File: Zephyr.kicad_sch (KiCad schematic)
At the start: 24 parts, among them J1 Conn_02x03_Counter_Clockwise, J11 Conn_01x03, SW4 SW_Push, U1 STM32F405RGT6, Y1 32.768KHz 12.5pF, Y2 8MHz 12pF

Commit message: Start ADC work
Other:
- added sheet ADC (adc_power.kicad_sch)
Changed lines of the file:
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@@
+	)
+	(sheet
+		(at 124.46 143.51)
+		(size 34.29 17.78)
+		(exclude_from_sim no)
+		(in_bom yes)
+		(on_board yes)
+		(dnp no)
+		(fields_autoplaced yes)
+		(stroke
+			(width 0.1524)
+			(type solid)
+		)
+		(fill
+			(color 0 0 0 0.0000)
+		)
+		(property "Sheetname" "ADC"
+			(at 124.46 142.7984 0)
+			(effects
+				(font
+					(size 1.27 1.27)
+				)
+				(justify left bottom)
+			)
+		)
+		(property "Sheetfile" "adc_power.kicad_sch"
+			(at 124.46 161.8746 0)
+			(effects
+				(font
+					(size 1.27 1.27)
+				)
+				(justify left top)
+			)
+		)
+		(instances
+			(project "Zephyr"
+				(path "/e99ca14d-cacc-4390-92ee-6dcff8e13ef3"
+					(page "5")
+				)
+			)
+		)
 	)
 	(sheet

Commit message: Continue work on power supply
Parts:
- added BZ1: Buzzer, symbol Device:Buzzer
- added H1, H2, H3, H4: MountingHole_Pad, MountingHole:MountingHole_3.2mm_M3_Pad, symbol Mechanical:MountingHole_Pad
- added J13: Conn_01x03, symbol Connector_Generic:Conn_01x03
- added J14: Conn_01x06, symbol Connector_Generic:Conn_01x06
- added Q1, Q2: MMBT3904, Package_TO_SOT_SMD:SOT-23, symbol Transistor_BJT:MMBT3904
- added R31: 1k, symbol Device:R
- added R32, R39: 10k, symbol Device:R
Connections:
- net +3.3V: now also J14.3 (Pin_3), R32.2
- net +5V: now also J13.2 (Pin_2), J14.2 (Pin_2), Q2.3 (C)
- net GND: now also BZ1.2 (-), H1.1, H2.1, H3.1, H4.1, J13.3 (Pin_3), J14.6 (Pin_6), Q1.2 (E), R39.2
- net SBUS_IN: now also R31.1
- net NEOPIXEL_OUT: now reaches R24.1
- net at D4.2 (DOUT): now also J13.1 (Pin_1)
- new net: Q1.1 (B), R31.2
- new net: BZ1.1 (+), Q2.2 (E)
- new net BUZZER: Q2.1 (B), R39.1
- new net DEBUG_RX: J14.4 (Pin_4)
- new net DEBUG_TX: J14.5 (Pin_5)
- new net SBUS_RX: Q1.3 (C), R32.1
- new net VBUS: J14.1 (Pin_1)
- no-connect marks 2 -> 1
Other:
- note added: "NeoPixel Out"
- note added: "SBUS IN"
- moved on the sheet: D4, D5, J11, R24

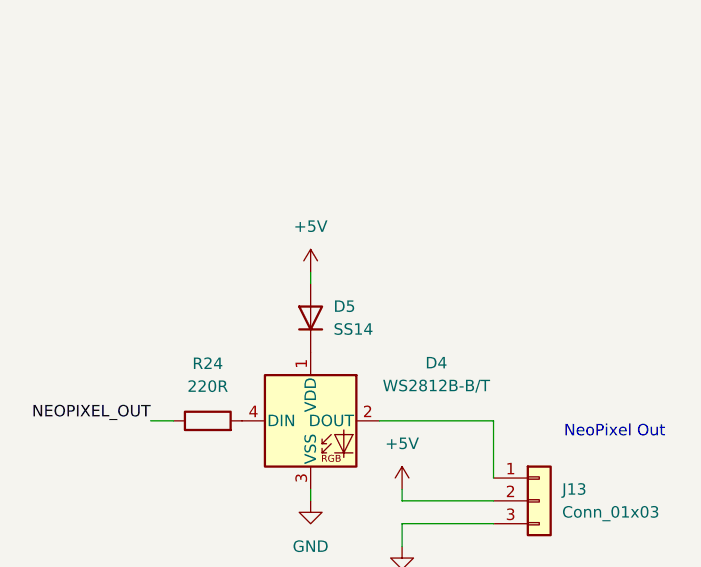
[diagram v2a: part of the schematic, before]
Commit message: 4.2V Regulator design
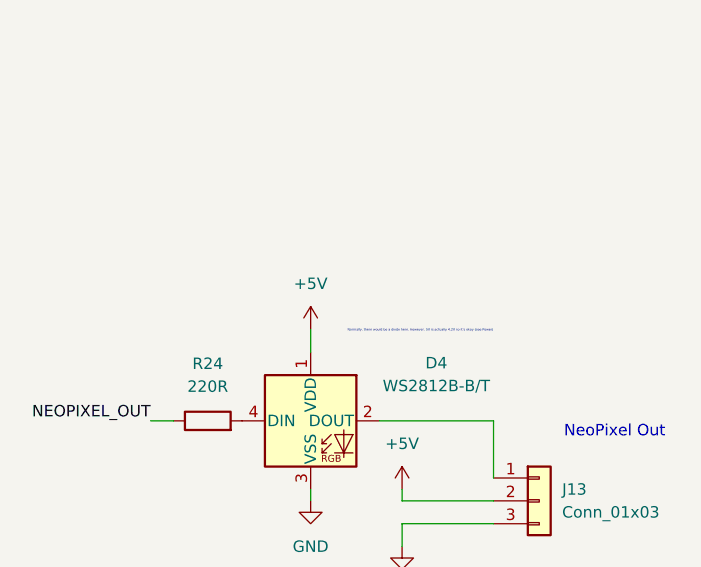
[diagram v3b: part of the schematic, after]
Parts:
- removed D5: SS14, symbol Device:D
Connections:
- net +5V: now also D4.1 (VDD)
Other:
- note added: "Normally, there would be a diode here. However, 5V is actually 4.2V so it's okay (see Power)"
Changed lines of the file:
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@@
 		)
 	)
+	(text "Normally, there would be a diode here. However, 5V is actually 4.2V so it's okay (see Power)"
+		(exclude_from_sim no)
+		(at 314.452 68.834 0)
+		(effects
+			(font
+				(size 0.254 0.254)
+			)
+		)
+	)
 	(text "NeoPixel Out"
 		(exclude_from_sim no)
@@
 	(wire
 		(pts
-			(xy 302.26 62.23) (xy 302.26 63.5)
+			(xy 302.26 68.58) (xy 302.26 71.12)
 		)
 		(stroke
@@
 	(symbol
 		(lib_id "power:+5V")
-		(at 302.26 62.23 0)
+		(at 302.26 68.58 0)
 		(unit 1)
 		(exclude_from_sim no)
@@
 		(fields_autoplaced yes)
 		(property "Reference" "#PWR093"
-			(at 302.26 66.04 0)
+			(at 302.26 72.39 0)
 			(effects
 				(font
@@
 		)
 		(property "Value" "+5V"
-			(at 302.26 57.15 0)
+			(at 302.26 63.5 0)
 			(effects
 				(font
@@
 		)
 		(property "Footprint" ""
-			(at 302.26 62.23 0)
+			(at 302.26 68.58 0)
 			(effects
 				(font
@@
 		)
 		(property "Datasheet" ""
-			(at 302.26 62.23 0)
+			(at 302.26 68.58 0)
 			(effects
 				(font
@@
 		)
 		(property "Description" "Power symbol creates a global label with name \"+5V\""
-			(at 302.26 62.23 0)
+			(at 302.26 68.58 0)
 			(effects
 				(font
@@
 					(unit 1)
 				)
-			)
-		)
-	)
-	(symbol
-		(lib_id "Device:D")
-		(at 302.26 67.31 90)
-		(unit 1)
-		(exclude_from_sim no)
-		(in_bom yes)
-		(on_board yes)
-		(dnp no)
-		(fields_autoplaced yes)
-		(property "Reference" "D5"
-			(at 304.8 66.0399 90)
-			(effects
-				(font
-					(size 1.27 1.27)
-				)
-				(justify right)
-			)
-		)
-		(property "Value" "SS14"
-			(at 304.8 68.5799 90)
-			(effects
-				(font
-					(size 1.27 1.27)
-				)
-				(justify right)
-			)
-		)
-		(property "Footprint" ""
-			(at 302.26 67.31 0)
-			(effects
-				(font
-					(size 1.27 1.27)
-				)
-				(hide yes)
-			)
-		)
-		(property "Datasheet" "~"
-			(at 302.26 67.31 0)
-			(effects
-				(font
-					(size 1.27 1.27)
-				)
-				(hide yes)
-			)
-		)
-		(property "Description" "Diode"
-			(at 302.26 67.31 0)
-			(effects
-				(font
-					(size 1.27 1.27)
-				)
-				(hide yes)
-			)
-		)
-		(property "Sim.Device" "D"
-			(at 302.26 67.31 0)
-			(effects
-				(font
-					(size 1.27 1.27)
-				)
-				(hide yes)
-			)
-		)
-		(property "Sim.Pins" "1=K 2=A"
-			(at 302.26 67.31 0)
-			(effects
-				(font
-					(size 1.27 1.27)
-				)
-				(hide yes)
-			)
-		)
-		(pin "1"
-		)
-		(pin "2"
-		)
-		(instances
-			(project "Zephyr"
-				(path "/e99ca14d-cacc-4390-92ee-6dcff8e13ef3"
-					(reference "D5")
-					(unit 1)
-				)

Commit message: Work on power supply...
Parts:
- added J15: Micro_SD_Card, symbol Connector:Micro_SD_Card
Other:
- moved on the sheet: BZ1, D4, J11, J13, Q1, Q2, R24, R31, R32, R39

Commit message: Add SD card
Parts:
- added C20: 100nF, Capacitor_SMD:C_0603_1608Metric_Pad1.08x0.95mm_HandSolder, symbol Device:C
- added R41, R42, R43, R44, R45, R46: 10k, symbol Device:R
- added U9: W25Q128JVS, Package_SO:SOIC-8_5.3x5.3mm_P1.27mm, symbol Memory_Flash:W25Q128JVS
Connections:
- net +3.3V: now also J15.4 (VDD), C20.1, R41.1, R42.1, R43.1, R44.1, R45.1, R46.1
- net GND: now also J15.6 (VSS), J15.9 (SHIELD), C20.2
- net at J15.1 (DAT2): now also R41.2
- net SD_CS: now reaches J15.2 (DAT3/CD)
- net SD_CS: now also R42.2
- net SD_MOSI: now reaches J15.3 (CMD)
- net SD_MOSI: now also R43.2
- net SD_SCK: now reaches J15.5 (CLK)
- net SD_SCK: now also R44.2
- net SD_MISO: now reaches J15.7 (DAT0)
- net SD_MISO: now also R45.2
- net at J15.8 (DAT1): now also R46.2
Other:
- note added: "Debug UART"

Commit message: Radio work
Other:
- added sheet Radio (radio.kicad_sch)
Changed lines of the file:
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@@
+		)
+	)
+	(sheet
+		(at 184.15 151.13)
+		(size 57.15 26.67)
+		(exclude_from_sim no)
+		(in_bom yes)
+		(on_board yes)
+		(dnp no)
+		(fields_autoplaced yes)
+		(stroke
+			(width 0.1524)
+			(type solid)
+		)
+		(fill
+			(color 0 0 0 0.0000)
+		)
+		(property "Sheetname" "Radio"
+			(at 184.15 150.4184 0)
+			(effects
+				(font
+					(size 1.27 1.27)
+				)
+				(justify left bottom)
+			)
+		)
+		(property "Sheetfile" "radio.kicad_sch"
+			(at 184.15 178.3846 0)
+			(effects
+				(font
+					(size 1.27 1.27)
+				)
+				(justify left top)
+			)
+		)
+		(instances
+			(project "Zephyr"
+				(path "/e99ca14d-cacc-4390-92ee-6dcff8e13ef3"
+					(page "6")
+				)
+			)
 		)
 	)

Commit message: SD card
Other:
- note added: "https://github.com/sbcshop/MicroSD-Breakout/blob/main/Hardware%20Files/SCH%20SD%20CARD%20BREAKOUT.pdf"
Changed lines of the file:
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@@
 	(generator_version "9.0")
 	(paper "A3")
+	(text "https://github.com/sbcshop/MicroSD-Breakout/blob/main/Hardware%20Files/SCH%20SD%20CARD%20BREAKOUT.pdf"
+		(exclude_from_sim no)
+		(at 346.964 171.704 0)
+		(effects
+			(font
+				(size 0.127 0.127)
+			)
+		)
+	)
 	(text "C51927445"
 		(exclude_from_sim no)

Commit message: More work... SD, flash, etc.
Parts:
- added C26: 100nF, Capacitor_SMD:C_0603_1608Metric_Pad1.08x0.95mm_HandSolder, symbol Device:C
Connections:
- net +3.3V: now also U9.3 (~{WP}/IO_{2}), U9.7 (~{HOLD}/~{RESET}/IO_{3}), U9.8 (VCC), C26.1
- net GND: now also U9.4 (GND), C26.2
- net CS_FLASH: now reaches U9.1 (~{CS})
- net MISO_FLASH: now reaches U9.2 (DO/IO_{1})
- net MOSI_FLASH: now reaches U9.5 (DI/IO_{0})
- net CLK_FLASH: now reaches U9.6 (CLK)
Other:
- sheet ADC ports: added ADC_0, ADC_1, ADC_2, ADC_3, ADC_4, ADC_5; removed none
- sheet Guidance Sensors ports: added BNO_RESET, IMU_DRDY, MAG_DRDY, RXD_GPS, SCL_I2C, SDA_I2C, TXD_GPS; removed none
- sheet Radio ports: added RF_BUSY, RF_DIO1, RF_MISO, RF_MOSI, RF_NSS, RF_RXEN, RF_SCK, RF_TXEN; removed none
- sheet Servo Driver ports: added SERVO_SCL, SERVO_SDA; removed none
